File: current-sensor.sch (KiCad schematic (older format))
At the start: 40 parts, among them J1 ‎0197134001‎, J2 ‎0197134001‎, J3 0731000105, J4 Molex_SL_01x02_Male, J5 Molex_SL_01x02_Male, SW1 PN12SHNA03QE, SW2 OS103011MA7QP1, SW3 OS103011MA7QP1, U1 ACS730xLCTR-20AB, U2 AD8616xRM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

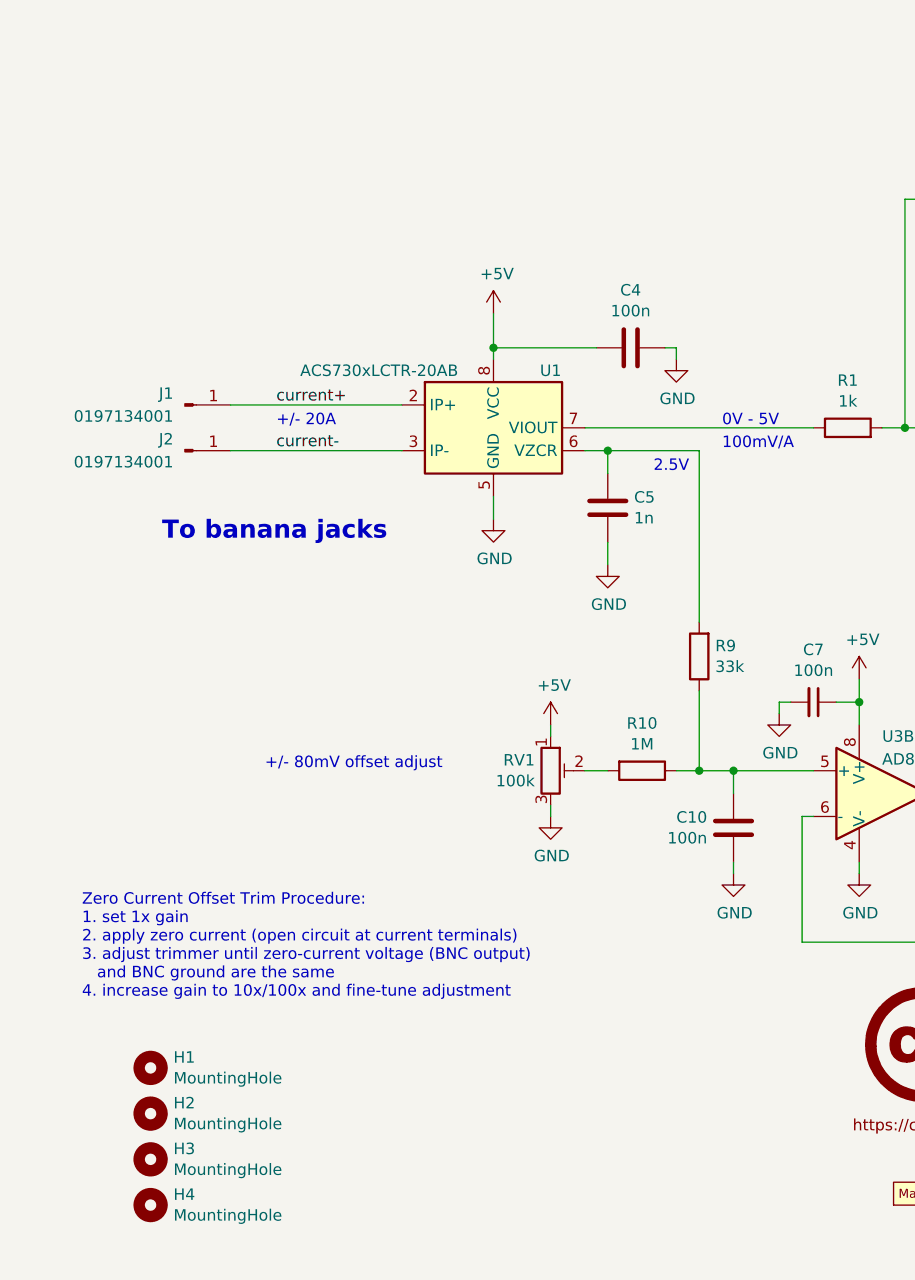
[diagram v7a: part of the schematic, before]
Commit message: Change offset trim circuit
completely ignore reference output from current sensor IC. Instead, use
trimpot to get 2.5V +/- 200mV reference voltage.
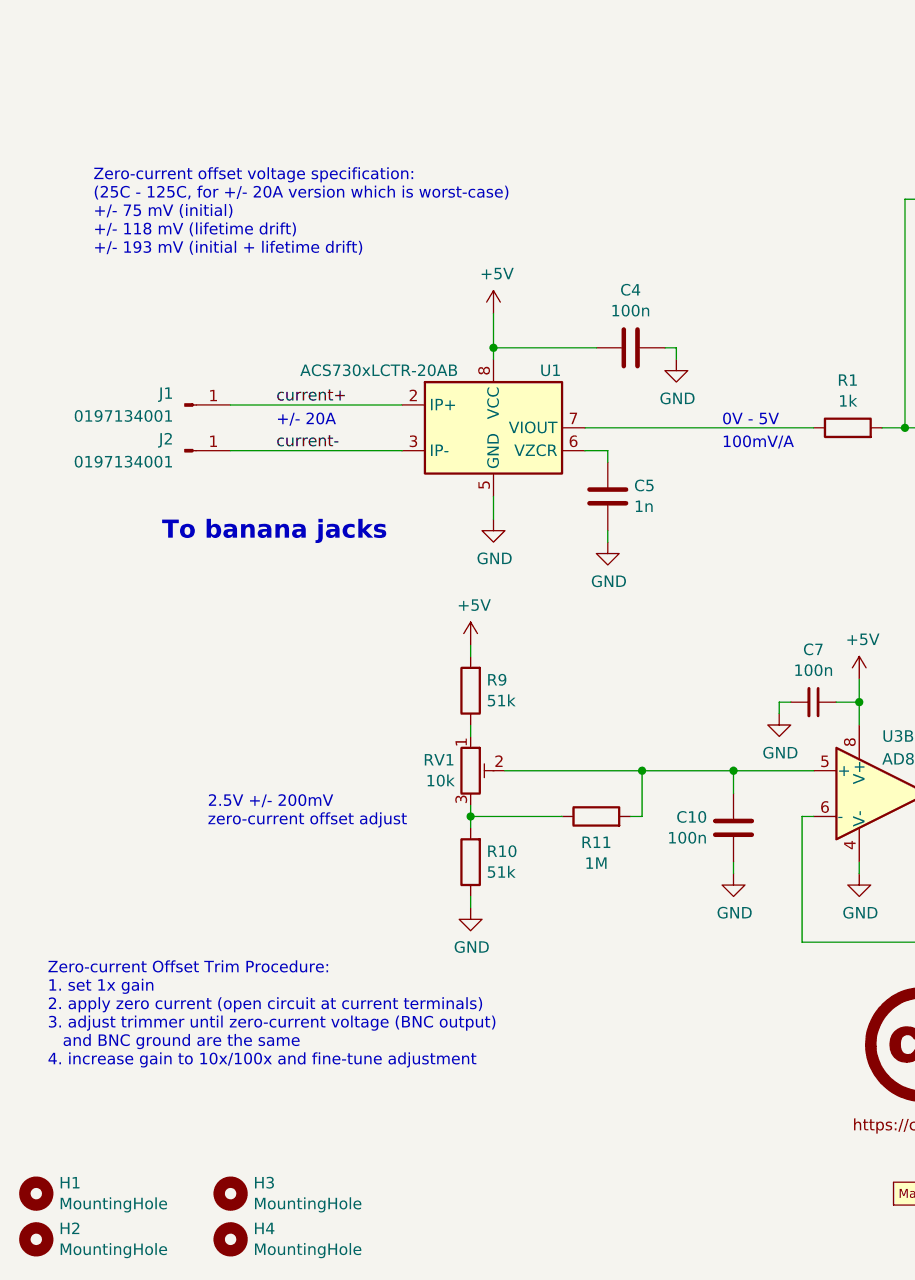
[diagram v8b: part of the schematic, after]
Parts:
- added R10: 51k, Resistor_SMD:R_0603_1608Metric, symbol Device:R
- R9: value 33k -> 51k
- RV1: value 100k -> 10k; Manufacturer PN TS53YL104MR10 -> TS53YL103MR10
- renumbered R10 to R11
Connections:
- net +5V: now also R9.2; no longer RV1.1
- net GND: now also R10.1; no longer RV1.3
- net at C5.1, U1.6 (VZCR): no longer R9.2
- net at C10.1, U3.5 (+): now also R11.2, RV1.2; no longer R11.1, R9.1
- new net: R9.1, RV1.1
- new net: R10.2, R11.1, RV1.3
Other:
- note added: "2.5V +/- 200mV\nzero-current offset adjust"
- note added: "Zero-current Offset Trim Procedure:\n1. set 1x gain\n2. apply zero current (open circuit at current terminals)\n3. adjust trimmer until zero-current voltage (BNC output)\n and BNC ground are the same\n4. increase gain to 10x/100x and fine-tune adjustment"
- note added: "Zero-current offset voltage specification:\n(25C - 125C, for +/- 20A version which is worst-case)\n+/- 75 mV (initial)\n+/- 118 mV (lifetime drift)\n+/- 193 mV (initial + lifetime drift)"
- note removed: "+/- 80mV offset adjust"
- note removed: "2.5V"
- note removed: "Zero Current Offset Trim Procedure:\n1. set 1x gain\n2. apply zero current (open circuit at current terminals)\n3. adjust trimmer until zero-current voltage (BNC output)\n and BNC ground are the same\n4. increase gain to 10x/100x and fine-tune adjustment"
- moved on the sheet: C5, H1, H2, H3, H4, R11, RV1
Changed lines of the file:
@@
 Sheet 1 1
 Title "Current Sensor"
-Date "2021-01-03"
+Date "2021-08-22"
 Rev "2"
 Comp "G. Keeth"
@@
 Connection ~ 5950 1300
 $Comp
-L Device:C C5
-U 1 1 5EFC8D89
-P 3100 4700
-F 0 "C5" H 3215 4746 50  0000 L CNN
-F 1 "1n" H 3215 4655 50  0000 L CNN
-F 2 "Capacitor_SMD:C_0603_1608Metric" H 3138 4550 50  0001 C CNN
-F 3 "~" H 3100 4700 50  0001 C CNN
-	1    3100 4700
-	1    0    0    -1
-$EndComp
-$Comp
 L power:GND #PWR0105
 U 1 1 5EFC981E
-P 3100 4950
-F 0 "#PWR0105" H 3100 4700 50  0001 C CNN
-F 1 "GND" H 3105 4777 50  0000 C CNN
-F 2 "" H 3100 4950 50  0001 C CNN
-F 3 "" H 3100 4950 50  0001 C CNN
-	1    3100 4950
-	1    0    0    -1
-$EndComp
-Wire Wire Line
-	3100 4850 3100 4950
+P 3100 4850
+F 0 "#PWR0105" H 3100 4600 50  0001 C CNN
+F 1 "GND" H 3105 4677 50  0000 C CNN
+F 2 "" H 3100 4850 50  0001 C CNN
+F 3 "" H 3100 4850 50  0001 C CNN
+	1    3100 4850
+	1    0    0    -1
+$EndComp
+Wire Wire Line
+	3100 4800 3100 4850
 $Comp
 L Device:C C4
@@
 Wire Wire Line
 	3000 4450 3100 4450
-Text Notes 3300 4550 0    50   ~ 0
-2.5V
 Text Notes 3600 4350 0    50   ~ 0
 0V - 5V
@@
 	4900 4550 4800 4550
 Wire Wire Line
-	4800 4550 4800 5950
-Wire Wire Line
 	7750 4550 7550 4550
 Connection ~ 7550 4550
@@
 	1    0    0    -1
 $EndComp
-Wire Wire Line
-	4200 5650 4200 5550
 $Comp
 L Device:C_Small C7
@@
 	0    1    1    0
 $EndComp
-Wire Wire Line
-	4100 5550 4200 5550
 Connection ~ 4200 5550
 Wire Wire Line
@@
 L Mechanical:MountingHole H1
 U 1 1 5F070491
-P 1100 7150
-F 0 "H1" H 1200 7196 50  0000 L CNN
-F 1 "MountingHole" H 1200 7105 50  0000 L CNN
-F 2 "MountingHole:MountingHole_3.2mm_M3" H 1100 7150 50  0001 C CNN
-F 3 "~" H 1100 7150 50  0001 C CNN
-	1    1100 7150
+P 600 7700
+F 0 "H1" H 700 7746 50  0000 L CNN
+F 1 "MountingHole" H 700 7655 50  0000 L CNN
+F 2 "MountingHole:MountingHole_3.2mm_M3" H 600 7700 50  0001 C CNN
+F 3 "~" H 600 7700 50  0001 C CNN
+	1    600  7700
 	1    0    0    -1
 $EndComp
@@
 L Mechanical:MountingHole H2
 U 1 1 5F072064
-P 1100 7350
-F 0 "H2" H 1200 7396 50  0000 L CNN
-F 1 "MountingHole" H 1200 7305 50  0000 L CNN
-F 2 "MountingHole:MountingHole_3.2mm_M3" H 1100 7350 50  0001 C CNN
-F 3 "~" H 1100 7350 50  0001 C CNN
-	1    1100 7350
+P 600 7900
+F 0 "H2" H 700 7946 50  0000 L CNN
+F 1 "MountingHole" H 700 7855 50  0000 L CNN
+F 2 "MountingHole:MountingHole_3.2mm_M3" H 600 7900 50  0001 C CNN
+F 3 "~" H 600 7900 50  0001 C CNN
+	1    600  7900
 	1    0    0    -1
 $EndComp
@@
 L Mechanical:MountingHole H3
 U 1 1 5F076197
-P 1100 7550
-F 0 "H3" H 1200 7596 50  0000 L CNN
-F 1 "MountingHole" H 1200 7505 50  0000 L CNN
-F 2 "MountingHole:MountingHole_3.2mm_M3" H 1100 7550 50  0001 C CNN
-F 3 "~" H 1100 7550 50  0001 C CNN
-	1    1100 7550
+P 1450 7700
+F 0 "H3" H 1550 7746 50  0000 L CNN
+F 1 "MountingHole" H 1550 7655 50  0000 L CNN
+F 2 "MountingHole:MountingHole_3.2mm_M3" H 1450 7700 50  0001 C CNN
+F 3 "~" H 1450 7700 50  0001 C CNN
+	1    1450 7700
 	1    0    0    -1
 $EndComp
@@
 L Mechanical:MountingHole H4
 U 1 1 5F0762C6
-P 1100 7750
-F 0 "H4" H 1200 7796 50  0000 L CNN
-F 1 "MountingHole" H 1200 7705 50  0000 L CNN
-F 2 "MountingHole:MountingHole_3.2mm_M3" H 1100 7750 50  0001 C CNN
-F 3 "~" H 1100 7750 50  0001 C CNN
-	1    1100 7750
+P 1450 7900
+F 0 "H4" H 1550 7946 50  0000 L CNN
+F 1 "MountingHole" H 1550 7855 50  0000 L CNN
+F 2 "MountingHole:MountingHole_3.2mm_M3" H 1450 7900 50  0001 C CNN
+F 3 "~" H 1450 7900 50  0001 C CNN
+	1    1450 7900
 	1    0    0    -1
 $EndComp
@@
 L Device:R_POT_TRIM RV1
 U 1 1 5FF299EA
-P 2850 5850
-F 0 "RV1" H 2781 5896 50  0000 R CNN
-F 1 "100k" H 2781 5805 50  0000 R CNN
-F 2 "Potentiometer_SMD:Potentiometer_Vishay_TS53YL_Vertical" H 2850 5850 50  0001 C CNN
-F 3 "~" H 2850 5850 50  0001 C CNN
-F 4 "Vishay Svernice" H 2850 5850 50  0001 C CNN "Manufacturer"
-F 5 "TS53YL104MR10" H 2850 5850 50  0001 C CNN "Manufacturer PN"
-	1    2850 5850
+P 2500 5850
+F 0 "RV1" H 2431 5896 50  0000 R CNN
+F 1 "10k" H 2431 5805 50  0000 R CNN
+F 2 "Potentiometer_SMD:Potentiometer_Vishay_TS53YL_Vertical" H 2500 5850 50  0001 C CNN
+F 3 "~" H 2500 5850 50  0001 C CNN
+F 4 "Vishay Svernice" H 2500 5850 50  0001 C CNN "Manufacturer"
+F 5 "TS53YL103MR10" H 2500 5850 50  0001 C CNN "Manufacturer PN"
+	1    2500 5850
 	1    0    0    -1
 $EndComp
@@
 L power:GND #PWR0119
 U 1 1 5FF2A0C5
-P 2850 6050
-F 0 "#PWR0119" H 2850 5800 50  0001 C CNN
-F 1 "GND" H 2855 5877 50  0000 C CNN
-F 2 "" H 2850 6050 50  0001 C CNN
-F 3 "" H 2850 6050 50  0001 C CNN
-	1    2850 6050
+P 2500 6450
+F 0 "#PWR0119" H 2500 6200 50  0001 C CNN
+F 1 "GND" H 2505 6277 50  0000 C CNN
+F 2 "" H 2500 6450 50  0001 C CNN
+F 3 "" H 2500 6450 50  0001 C CNN
+	1    2500 6450
 	1    0    0    -1
 $EndComp
@@
 L power:+5V #PWR0120
 U 1 1 5FF2A4DA
-P 2850 5650
-F 0 "#PWR0120" H 2850 5500 50  0001 C CNN
-F 1 "+5V" H 2865 5823 50  0000 C CNN
-F 2 "" H 2850 5650 50  0001 C CNN
-F 3 "" H 2850 5650 50  0001 C CNN
-	1    2850 5650
-	1    0    0    -1
-$EndComp
-$Comp
-L Device:R R10
+P 2500 5300
+F 0 "#PWR0120" H 2500 5150 50  0001 C CNN
+F 1 "+5V" H 2515 5473 50  0000 C CNN
+F 2 "" H 2500 5300 50  0001 C CNN
+F 3 "" H 2500 5300 50  0001 C CNN
+	1    2500 5300
+	1    0    0    -1
+$EndComp
+$Comp
+L Device:R R11
 U 1 1 5FF35394
-P 3250 5850
-F 0 "R10" V 3043 5850 50  0000 C CNN
-F 1 "1M" V 3134 5850 50  0000 C CNN
-F 2 "Resistor_SMD:R_0603_1608Metric" V 3180 5850 50  0001 C CNN
-F 3 "~" H 3250 5850 50  0001 C CNN
-	1    3250 5850
-	0    1    1    0
-$EndComp
-Wire Wire Line
-	3000 5850 3100 5850
-$Comp
-L Device:R R9
-U 1 1 5FF44480
-P 3500 5350
-F 0 "R9" H 3430 5304 50  0000 R CNN
-F 1 "33k" H 3430 5395 50  0000 R CNN
-F 2 "Resistor_SMD:R_0603_1608Metric" V 3430 5350 50  0001 C CNN
-F 3 "~" H 3500 5350 50  0001 C CNN
-	1    3500 5350
-	-1   0    0    1
-$EndComp
-Wire Wire Line
-	3100 4450 3500 4450
-Wire Wire Line
-	3500 4450 3500 5200
-Connection ~ 3100 4450
-Wire Wire Line
-	3100 4450 3100 4550
-Wire Wire Line
-	3400 5850 3500 5850
-Wire Wire Line
-	3500 5850 3500 5500
-Wire Wire Line
-	3500 5850 3650 5850
-Connection ~ 3500 5850
-Text Notes 800  6850 0    50   ~ 0
-Zero Current Offset Trim Procedure:\n1. set 1x gain\n2. apply zero current (open circuit at current terminals)\n3. adjust trimmer until zero-current voltage (BNC output)\n   and BNC ground are the same\n4. increase gain to 10x/100x and fine-tune adjustment
-Text Notes 1600 5850 0    50   ~ 0
-+/- 80mV offset adjust
-Wire Wire Line
-	2850 5700 2850 5650
-Wire Wire Line
-	2850 6000 2850 6050
+P 3050 6050
+F 0 "R11" V 2935 6050 50  0000 C CNN
+F 1 "1M" V 2844 6050 50  0000 C CNN
+F 2 "Resistor_SMD:R_0603_1608Metric" V 2980 6050 50  0001 C CNN
+F 3 "~" H 3050 6050 50  0001 C CNN
+	1    3050 6050
+	0    -1   -1   0
+$EndComp
+Text Notes 650  7150 0    50   ~ 0
+Zero-current Offset Trim Procedure:\n1. set 1x gain\n2. apply zero current (open circuit at current terminals)\n3. adjust trimmer until zero-current voltage (BNC output)\n   and BNC ground are the same\n4. increase gain to 10x/100x and fine-tune adjustment
+Text Notes 1350 6100 0    50   ~ 0
+2.5V +/- 200mV\nzero-current offset adjust
+Wire Wire Line
+	2500 5700 2500 5650
+Wire Wire Line
+	2500 6000 2500 6050
 $Comp
 L Device:C C10
@@
 	3650 5950 3650 5850
 Connection ~ 3650 5850
+Text Notes 850  3600 0    50   ~ 0
+Zero-current offset voltage specification:\n(25C - 125C, for +/- 20A version which is worst-case)\n+/- 75 mV (initial)\n+/- 118 mV (lifetime drift)\n+/- 193 mV (initial + lifetime drift)
+Wire Wire Line
+	2500 5350 2500 5300
+Wire Wire Line
+	2500 6450 2500 6400
+Connection ~ 3250 5850
+Wire Wire Line
+	3250 5850 3650 5850
+Wire Wire Line
+	3100 4450 3100 4500
+$Comp
+L Device:C C5
+U 1 1 5EFC8D89
+P 3100 4650
+F 0 "C5" H 3215 4696 50  0000 L CNN
+F 1 "1n" H 3215 4605 50  0000 L CNN
+F 2 "Capacitor_SMD:C_0603_1608Metric" H 3138 4500 50  0001 C CNN
+F 3 "~" H 3100 4650 50  0001 C CNN
+	1    3100 4650
+	1    0    0    -1
+$EndComp
+Wire Wire Line
+	2650 5850 3250 5850
+Wire Wire Line
+	3200 6050 3250 6050
+Wire Wire Line
+	3250 5850 3250 6050
+Wire Wire Line
+	2900 6050 2500 6050
+Connection ~ 2500 6050
+Wire Wire Line
+	2500 6050 2500 6100
+Wire Wire Line
+	4200 5650 4200 5550
 Wire Wire Line
 	3650 5850 4000 5850
+Wire Wire Line
+	4100 5550 4200 5550
+Wire Wire Line
+	4800 4550 4800 5950
+$Comp
+L Device:R R10
+U 1 1 6124FAA4
+P 2500 6250
+F 0 "R10" H 2430 6204 50  0000 R CNN
+F 1 "51k" H 2430 6295 50  0000 R CNN
+F 2 "Resistor_SMD:R_0603_1608Metric" V 2430 6250 50  0001 C CNN
+F 3 "~" H 2500 6250 50  0001 C CNN
+	1    2500 6250
+	-1   0    0    1
+$EndComp
+$Comp
+L Device:R R9
+U 1 1 6123D28E
+P 2500 5500
+F 0 "R9" H 2430 5454 50  0000 R CNN
+F 1 "51k" H 2430 5545 50  0000 R CNN
+F 2 "Resistor_SMD:R_0603_1608Metric" V 2430 5500 50  0001 C CNN
+F 3 "~" H 2500 5500 50  0001 C CNN
+	1    2500 5500
+	-1   0    0    1
+$EndComp
 $EndSCHEMATC
